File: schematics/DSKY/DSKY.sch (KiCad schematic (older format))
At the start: 0 parts

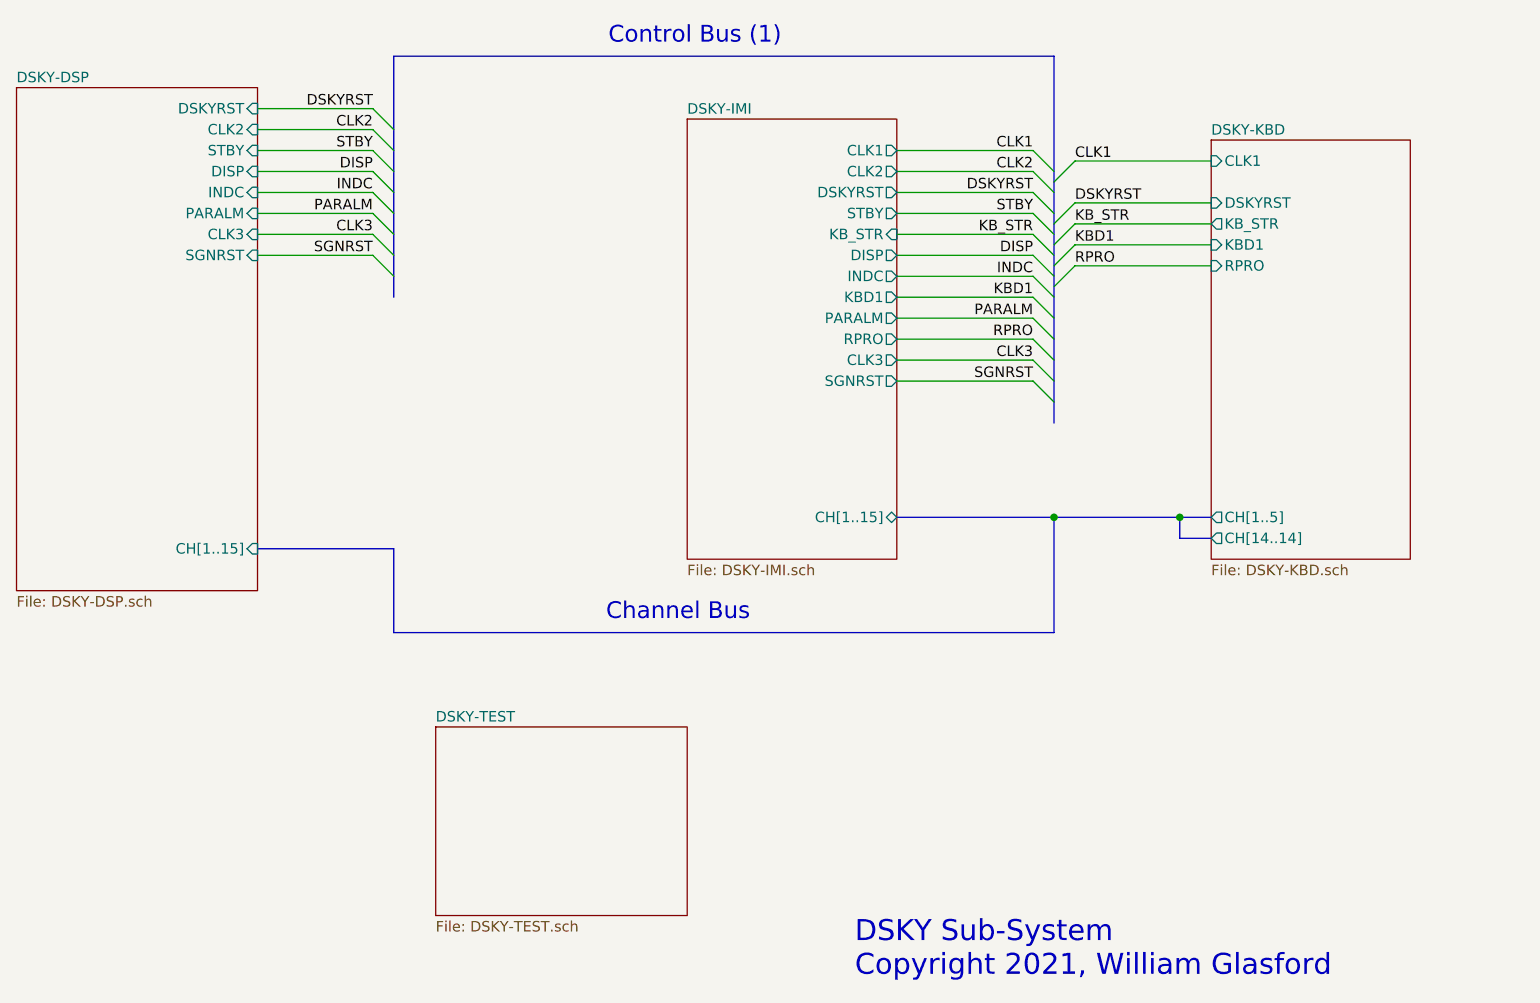
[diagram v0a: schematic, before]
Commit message: Using 4 LED driver chips.
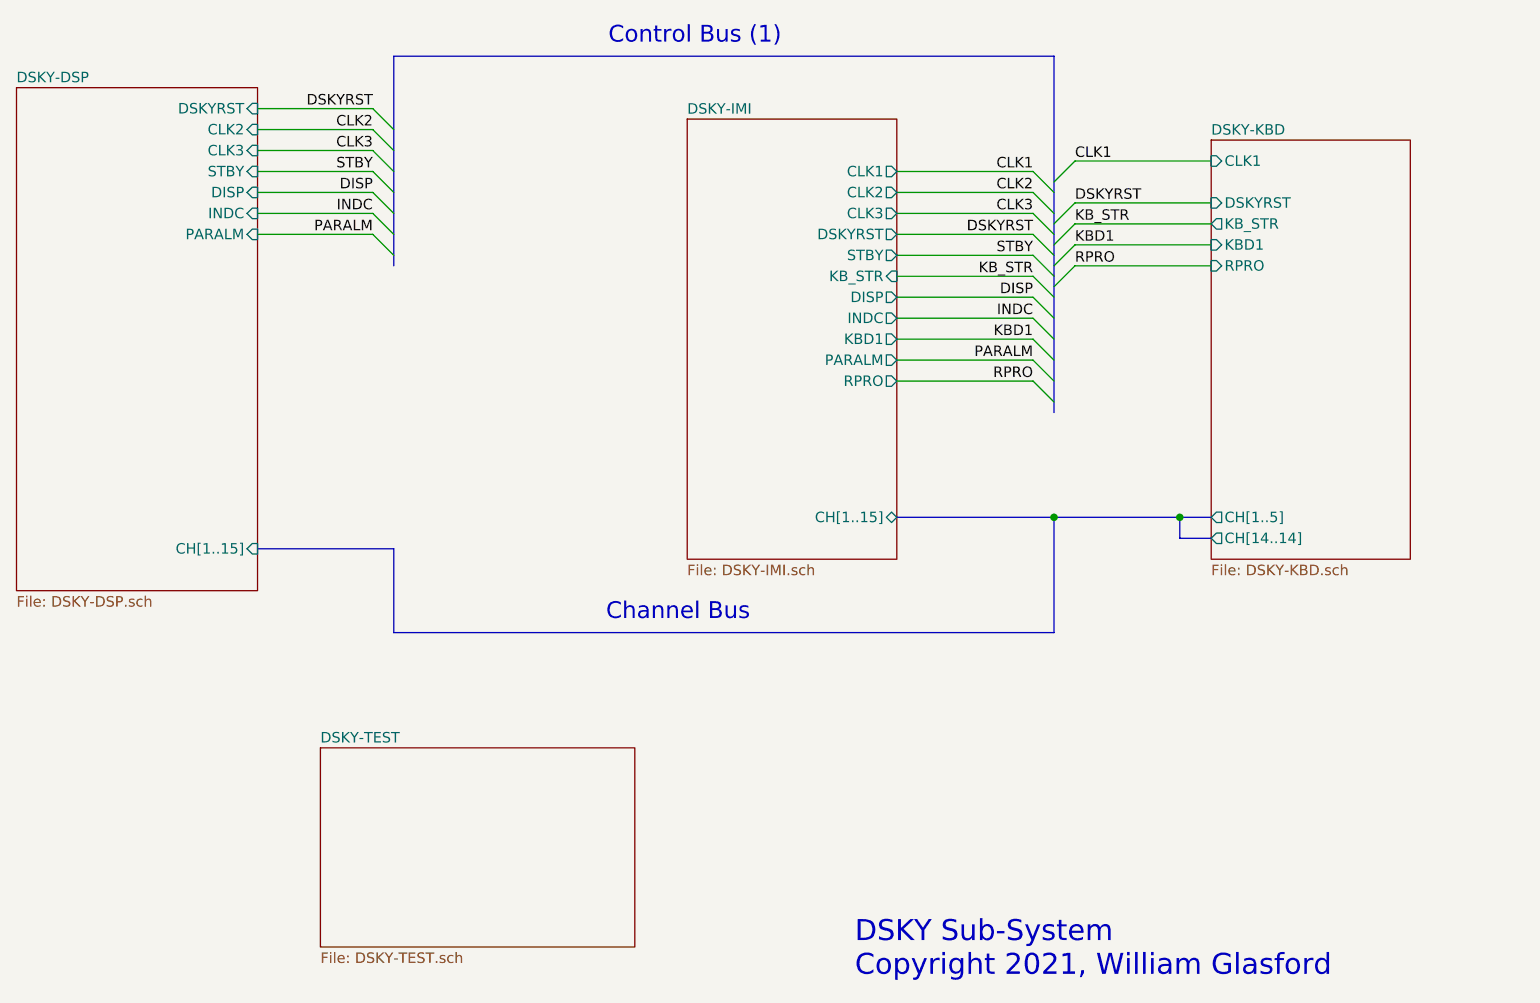
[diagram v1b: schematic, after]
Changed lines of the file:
@@
 $Descr A 11000 8500
 encoding utf-8
-Sheet 1 15
+Sheet 1 13
 Title ""
 Date ""
@@
 $EndDescr
 Entry Wire Line
+	7250 3500 7350 3600
+Wire Wire Line
+	6600 3500 7250 3500
+Entry Wire Line
 	7350 3550 7450 3450
 Wire Wire Line
@@
 Text Label 7450 3450 0    50   ~ 0
 DSKYRST
+Text Label 7250 3600 2    50   ~ 0
+DSKYRST
+Wire Wire Line
+	6600 3400 7250 3400
+Entry Wire Line
+	7250 3400 7350 3500
 Text Label 7250 3400 2    50   ~ 0
-DSKYRST
+CLK2
+Wire Wire Line
+	3550 3300 4100 3300
+Entry Wire Line
+	4100 3300 4200 3400
+Text Label 4100 3500 2    50   ~ 0
+INDC
 Wire Wire Line
 	6600 3300 7250 3300
@@
 	7250 3300 7350 3400
 Text Label 7250 3300 2    50   ~ 0
-CLK2
-Wire Wire Line
-	3550 3200 4100 3200
-Entry Wire Line
-	4100 3200 4200 3300
-Text Label 4100 3400 2    50   ~ 0
-INDC
-Wire Wire Line
-	6600 3200 7250 3200
-Entry Wire Line
-	7250 3200 7350 3300
-Text Label 7250 3200 2    50   ~ 0
 CLK1
 Wire Wire Line
-	6600 3400 7250 3400
-Wire Wire Line
-	6600 3500 7250 3500
-Entry Wire Line
-	7250 3400 7350 3500
-Entry Wire Line
-	7250 3500 7350 3600
-Text Label 7250 3600 2    50   ~ 0
+	6600 3600 7250 3600
+Wire Wire Line
+	6600 3700 7250 3700
+Entry Wire Line
+	7250 3600 7350 3700
+Entry Wire Line
+	7250 3700 7350 3800
+Text Label 7250 3800 2    50   ~ 0
 KB_STR
-Text Label 7250 3700 2    50   ~ 0
+Text Label 7250 3900 2    50   ~ 0
 DISP
 Text Notes 6050 2700 2    80   ~ 0
@@
 	4200 5500 7350 5500
 Wire Wire Line
-	6600 3600 7250 3600
-Entry Wire Line
-	7250 3600 7350 3700
-Text Label 7250 3800 2    50   ~ 0
+	6600 3800 7250 3800
+Entry Wire Line
+	7250 3800 7350 3900
+Text Label 7250 4000 2    50   ~ 0
 INDC
-Text Label 4100 3200 2    50   ~ 0
+Text Label 4100 3300 2    50   ~ 0
 STBY
+Entry Wire Line
+	4200 3300 4100 3200
 Entry Wire Line
 	4200 3200 4100 3100
@@
 Text Label 4100 3000 2    50   ~ 0
 DSKYRST
-Text Label 4100 3300 2    50   ~ 0
+Text Label 4100 3400 2    50   ~ 0
 DISP
 Wire Wire Line
@@
 Wire Wire Line
 	3550 3100 4100 3100
+Wire Wire Line
+	3550 3200 4100 3200
+Wire Wire Line
+	6600 3900 7250 3900
+Entry Wire Line
+	7250 3900 7350 4000
+Text Label 7250 4100 2    50   ~ 0
+KBD1
+Wire Wire Line
+	6600 4000 7250 4000
+Entry Wire Line
+	7250 4000 7350 4100
+Text Label 7250 4200 2    50   ~ 0
+PARALM
+Wire Wire Line
+	8100 3550 7450 3550
+Entry Wire Line
+	7350 3650 7450 3550
+Text Label 7450 3550 0    50   ~ 0
+KB_STR
+Text Label 7250 3700 2    50   ~ 0
+STBY
+Wire Wire Line
+	8100 3650 7450 3650
+Entry Wire Line
+	7350 3750 7450 3650
+Wire Bus Line
+	4200 2750 7350 2750
+Wire Bus Line
+	3550 5100 4200 5100
+Wire Bus Line
+	4200 5100 4200 5500
+Wire Bus Line
+	7350 4950 7350 5500
+Wire Bus Line
+	6600 4950 7350 4950
+Connection ~ 7350 4950
+Wire Bus Line
+	7350 4950 7950 4950
+Text Label 7450 3650 0    50   ~ 0
+KBD1
+Entry Wire Line
+	7350 3350 7450 3250
+Text Label 7450 3250 0    50   ~ 0
+CLK1
+Wire Wire Line
+	8100 3250 7450 3250
+Entry Wire Line
+	4200 3500 4100 3400
+Text Label 4100 3600 2    50   ~ 0
+PARALM
+Wire Wire Line
+	3550 3400 4100 3400
+Wire Bus Line
+	8100 5050 7950 5050
+Wire Bus Line
+	7950 5050 7950 4950
+Connection ~ 7950 4950
+Wire Bus Line
+	7950 4950 8100 4950
+Text Notes 6400 7150 0    100  ~ 0
+DSKY Sub-System\nCopyright 2021, William Glasford
+Wire Wire Line
+	6600 4100 7250 4100
+Entry Wire Line
+	7250 4100 7350 4200
+Entry Wire Line
+	4200 3600 4100 3500
+Wire Wire Line
+	3550 3500 4100 3500
+Wire Wire Line
+	6600 4200 7250 4200
+Entry Wire Line
+	7250 4200 7350 4300
+Text Label 7250 4300 2    50   ~ 0
+RPRO
+Entry Wire Line
+	7350 3850 7450 3750
+Text Label 7450 3750 0    50   ~ 0
+RPRO
+Wire Wire Line
+	8100 3750 7450 3750
+Wire Wire Line
+	6600 4300 7250 4300
+Entry Wire Line
+	7250 4300 7350 4400
+Entry Wire Line
+	4200 3700 4100 3600
+Wire Wire Line
+	3550 3600 4100 3600
+Text Label 7250 3500 2    50   ~ 0
+CLK3
+Text Label 4100 3200 2    50   ~ 0
+CLK3
+$Sheet
+S 2400 2900 1150 2400
+U 60F98A64
+F0 "DSKY-DSP" 50
+F1 "DSKY-DSP.sch" 50
+F2 "DSKYRST" I R 3550 3000 50
+F3 "CLK2" I R 3550 3100 50
+F4 "CH[1..15]" I R 3550 5100 50
+F5 "STBY" I R 3550 3300 50
+F6 "PARALM" I R 3550 3600 50
+F7 "DISP" I R 3550 3400 50
+F8 "INDC" I R 3550 3500 50
+F9 "CLK3" I R 3550 3200 50
+$EndSheet
+$Sheet
+S 3850 6050 1500 950
+U 62ECFB9F
+F0 "DSKY-TEST" 50
+F1 "DSKY-TEST.sch" 50
+$EndSheet
 $Sheet
 S 5600 3050 1000 2100
@@
 F0 "DSKY-IMI" 50
 F1 "DSKY-IMI.sch" 50
-F2 "CLK2" O R 6600 3300 50
-F3 "DSKYRST" O R 6600 3400 50
-F4 "CLK1" O R 6600 3200 50
-F5 "STBY" O R 6600 3500 50
-F6 "PARALM" O R 6600 4000 50
-F7 "KB_STR" I R 6600 3600 50
+F2 "CLK2" O R 6600 3400 50
+F3 "DSKYRST" O R 6600 3600 50
+F4 "CLK1" O R 6600 3300 50
+F5 "STBY" O R 6600 3700 50
+F6 "PARALM" O R 6600 4200 50
+F7 "KB_STR" I R 6600 3800 50
 F8 "CH[1..15]" B R 6600 4950 50
-F9 "KBD1" O R 6600 3900 50
-F10 "DISP" O R 6600 3700 50
-F11 "INDC" O R 6600 3800 50
-F12 "RPRO" O R 6600 4100 50
-F13 "CLK3" O R 6600 4200 50
-F14 "SGNRST" O R 6600 4300 50
-$EndSheet
-Wire Wire Line
-	6600 3700 7250 3700
-Entry Wire Line
-	7250 3700 7350 3800
-Text Label 7250 3900 2    50   ~ 0
-KBD1
-Wire Wire Line
-	6600 3800 7250 3800
-Entry Wire Line
-	7250 3800 7350 3900
-Text Label 7250 4000 2    50   ~ 0
-PARALM
-Wire Wire Line
-	8100 3550 7450 3550
-Entry Wire Line
-	7350 3650 7450 3550
-Text Label 7450 3550 0    50   ~ 0
-KB_STR
-Text Label 7250 3500 2    50   ~ 0
-STBY
-Wire Wire Line
-	8100 3650 7450 3650
-Entry Wire Line
-	7350 3750 7450 3650
-Wire Bus Line
-	4200 2750 7350 2750
-Wire Bus Line
-	3550 5100 4200 5100
-Wire Bus Line
-	4200 5100 4200 5500
-Wire Bus Line
-	7350 4950 7350 5500
-Wire Bus Line
-	6600 4950 7350 4950
-Connection ~ 7350 4950
-Wire Bus Line
-	7350 4950 7950 4950
-Text Label 7450 3650 0    50   ~ 0
-KBD1
+F9 "KBD1" O R 6600 4100 50
+F10 "DISP" O R 6600 3900 50
+F11 "INDC" O R 6600 4000 50
+F12 "RPRO" O R 6600 4300 50
+F13 "CLK3" O R 6600 3500 50
+$EndSheet
 $Sheet
 S 8100 3150 950  2000
@@
 F8 "RPRO" I L 8100 3750 50
 $EndSheet
-Entry Wire Line
-	7350 3350 7450 3250
-Text Label 7450 3250 0    50   ~ 0
-CLK1
-Wire Wire Line
-	8100 3250 7450 3250
-Entry Wire Line
-	4200 3400 4100 3300
-Text Label 4100 3500 2    50   ~ 0
-PARALM
-Wire Wire Line
-	3550 3300 4100 3300
-Wire Bus Line
-	8100 5050 7950 5050
-Wire Bus Line
-	7950 5050 7950 4950
-Connection ~ 7950 4950
-Wire Bus Line
-	7950 4950 8100 4950
-Text Notes 6400 7150 0    100  ~ 0
-DSKY Sub-System\nCopyright 2021, William Glasford
-Wire Wire Line
-	6600 3900 7250 3900
-Entry Wire Line
-	7250 3900 7350 4000
-Entry Wire Line
-	4200 3500 4100 3400
-Wire Wire Line
-	3550 3400 4100 3400
-Wire Wire Line
-	6600 4000 7250 4000
-Entry Wire Line
-	7250 4000 7350 4100
-Text Label 7250 4100 2    50   ~ 0
-RPRO
-Entry Wire Line
-	7350 3850 7450 3750
-Text Label 7450 3750 0    50   ~ 0
-RPRO
-Wire Wire Line
-	8100 3750 7450 3750
-Wire Wire Line
-	6600 4100 7250 4100
-Entry Wire Line
-	7250 4100 7350 4200
-Entry Wire Line
-	4200 3600 4100 3500
-Wire Wire Line
-	3550 3500 4100 3500
-$Sheet
-S 2400 2900 1150 2400
-U 60F98A64
-F0 "DSKY-DSP" 50
-F1 "DSKY-DSP.sch" 50
-F2 "DSKYRST" I R 3550 3000 50
-F3 "CLK2" I R 3550 3100 50
-F4 "CH[1..15]" I R 3550 5100 50
-F5 "STBY" I R 3550 3200 50
-F6 "PARALM" I R 3550 3500 50
-F7 "DISP" I R 3550 3300 50
-F8 "INDC" I R 3550 3400 50
-F9 "CLK3" I R 3550 3600 50
-F10 "SGNRST" I R 3550 3700 50
-$EndSheet
-Wire Wire Line
-	6600 4200 7250 4200
-Entry Wire Line
-	7250 4200 7350 4300
-Text Label 7250 4200 2    50   ~ 0
-CLK3
-Entry Wire Line
-	4200 3700 4100 3600
-Text Label 4100 3600 2    50   ~ 0
-CLK3
-Wire Wire Line
-	3550 3600 4100 3600
-$Sheet
-S 4400 5950 1200 900
-U 6A27E71F
-F0 "DSKY-TEST" 50
-F1 "DSKY-TEST.sch" 50
-$EndSheet
-Wire Wire Line
-	6600 4300 7250 4300
-Entry Wire Line
-	7250 4300 7350 4400
-Text Label 7250 4300 2    50   ~ 0
-SGNRST
-Entry Wire Line
-	4200 3800 4100 3700
-Text Label 4100 3700 2    50   ~ 0
-SGNRST
-Wire Wire Line
-	3550 3700 4100 3700
-Wire Bus Line
-	4200 2750 4200 3900
-Wire Bus Line
-	7350 2750 7350 4500
+Wire Bus Line
+	4200 2750 4200 3750
+Wire Bus Line
+	7350 2750 7350 4450
 $EndSCHEMATC
